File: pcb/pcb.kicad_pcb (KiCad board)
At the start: 2 copper layers, 100 x 70 mm, 20 parts, among them K1 GENERIC_RELAY, K2 GENERIC_RELAY, Q1 BC547, Q2 BC547

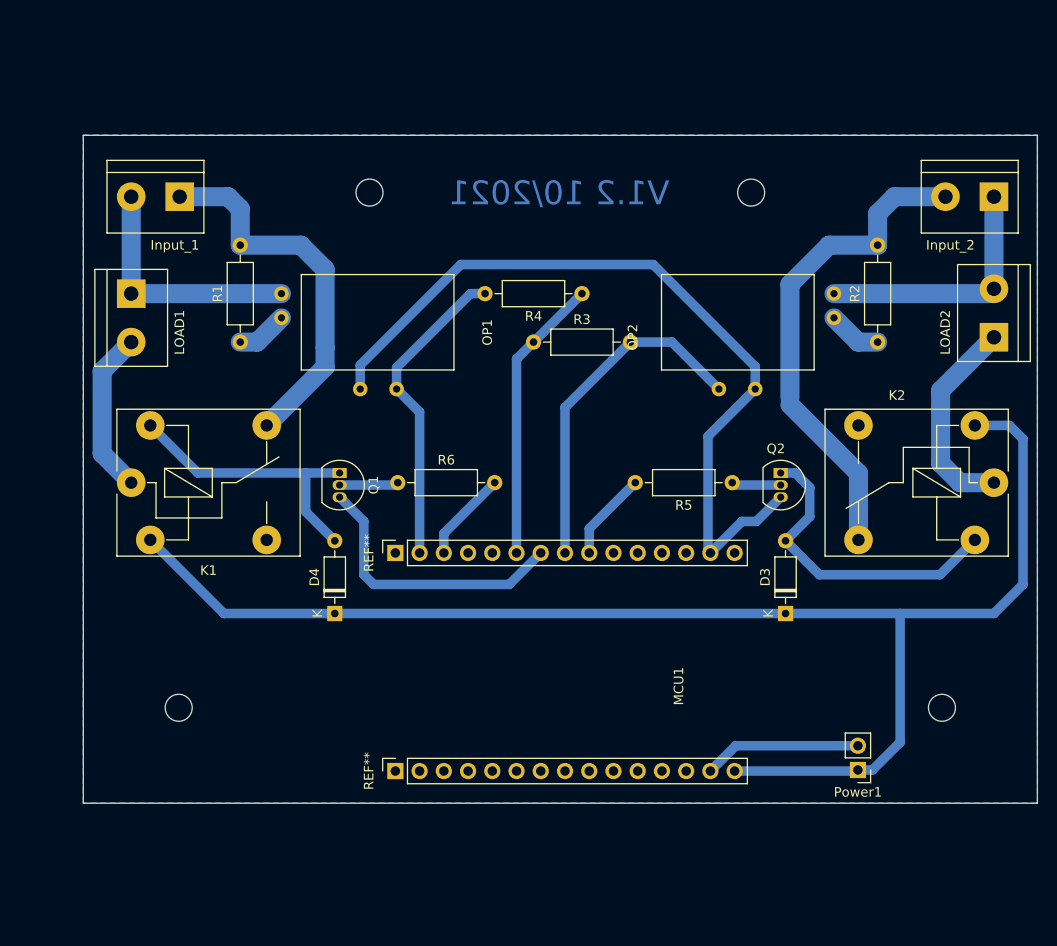
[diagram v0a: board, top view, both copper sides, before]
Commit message: Add new terminal block model and update PCB design
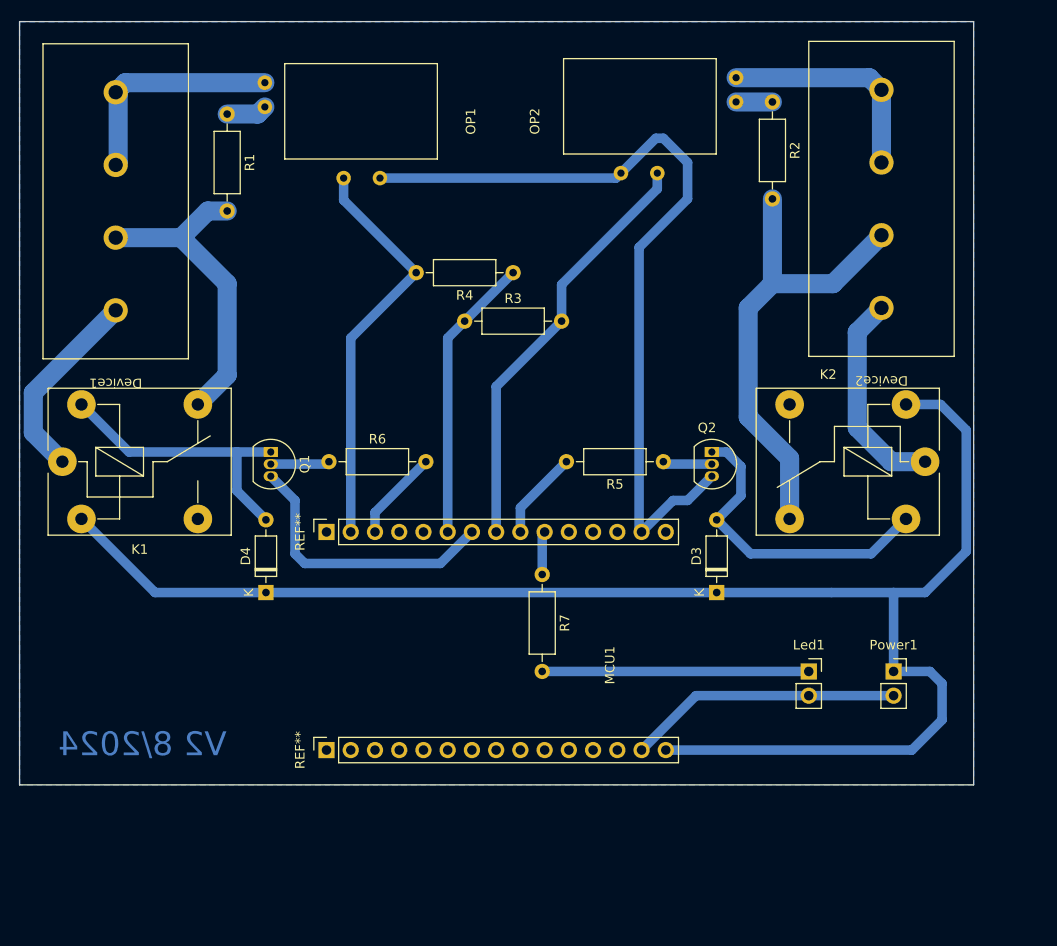
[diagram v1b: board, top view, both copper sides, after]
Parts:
- removed Input_1, Input_2, LOAD1, LOAD2: Conn_01x02, TerminalBlock:TerminalBlock_bornier-2_P5.08mm
- added Device1: Conn_01x04, Custom_Footprints:TerminalBlock_1x04, F.Cu at (100.1, 68.8)
- added Device2: Conn_01x04, Custom_Footprints:TerminalBlock_1x04, F.Cu at (180.3, 68.6)
- added Led1: Conn_01x02, Connector_PinSocket_2.54mm:PinSocket_1x02_P2.54mm_Vertical, F.Cu at (172.7, 118.1)
- added R7: 220, Resistor_THT:R_Axial_DIN0207_L6.3mm_D2.5mm_P10.16mm_Horizontal, F.Cu at (144.8, 108.0)
- K1, K2: value GENERIC_RELAY -> Generic_Relay
- Power1: footprint Connector_PinHeader_2.54mm:PinHeader_1x02_P2.54mm_Vertical -> Connector_PinSocket_2.54mm:PinSocket_1x02_P2.54mm_Vertical
- moved R2 27.5 mm to (168.9, 58.4), turned to -90 degrees
- moved OP2 24.9 mm to (147.3, 55.9)
- moved R1 23.9 mm to (111.8, 59.7), turned to -90 degrees
- moved OP1 22.2 mm to (134.0, 67.6)
- moved Power1 11.0 mm to (181.6, 118.1), turned to 0 degrees
- moved D4 7.54 mm to (115.8, 109.8)
- moved Q1 7.54 mm to (116.3, 95.1)
- moved Q2 7.54 mm to (162.6, 95.1)
- moved R4 7.54 mm to (141.7, 76.3)
- moved MCU1 7.54 mm to (151.4, 117.5)
- moved R3 7.54 mm to (136.7, 81.4)
- moved R5 7.54 mm to (157.5, 96.1)
- moved R6 7.54 mm to (122.4, 96.1)
- moved K1 7.54 mm to (94.5, 96.1)
- moved D3 7.54 mm to (163.1, 109.8)
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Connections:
- MCU1 pad 17: Net-(OP1-LDR2) -> Net-(OP1-LDR1)
- MCU1 pad 21: unconnected-(MCU1-D7-Pad21) -> Net-(MCU1-D7)
- OP1 pad 1: Net-(MCU1-D1) -> Net-(OP1-LDR1)
- OP1 pad 2: Net-(OP1-LDR2) -> Net-(MCU1-D1)
- OP2 pad 1: Net-(MCU1-D5) -> Net-(OP1-LDR1)
- OP2 pad 2: Net-(OP1-LDR2) -> Net-(MCU1-D5)
- Q2 pad 3: Net-(OP1-LDR2) -> Net-(OP1-LDR1)
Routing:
- net Net-(OP1-LDR1): track 0.00 -> 85.7 mm
- net Net-(OP1-LDR2): track 84.2 -> 0.00 mm
- net Net-(Led1-Pin_1): track 0.00 -> 27.9 mm
- net Net-(D3-K): track 148.9 -> 165.8 mm
- net Net-(Led1-Pin_2): track 16.6 -> 28.8 mm
- net Net-(MCU1-D1): track 32.9 -> 43.1 mm
- net Net-(MCU1-D5): track 36.2 -> 44.6 mm
- net Net-(Device1-Pin_3): track 39.5 -> 33.6 mm
- net Net-(MCU1-D7): track 0.00 -> 4.56 mm
- net Net-(Device1-Pin_4): track 17.3 -> 20.7 mm
- net Net-(Device2-Pin_1): track 26.6 -> 23.4 mm
- net Net-(Device1-Pin_1): track 25.9 -> 23.9 mm
- net Net-(Device2-Pin_3): track 51.8 -> 49.9 mm
- net Net-(OP2-IN1): track 5.62 -> 3.81 mm
- net Net-(OP1-IN1): track 5.37 -> 4.26 mm
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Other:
- board size 100 x 70 mm -> 100 x 80 mm
- board text added: "V2 8/2024"
- board text removed: "V1.2 10/2021"

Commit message: Add pin socket model and update PCB
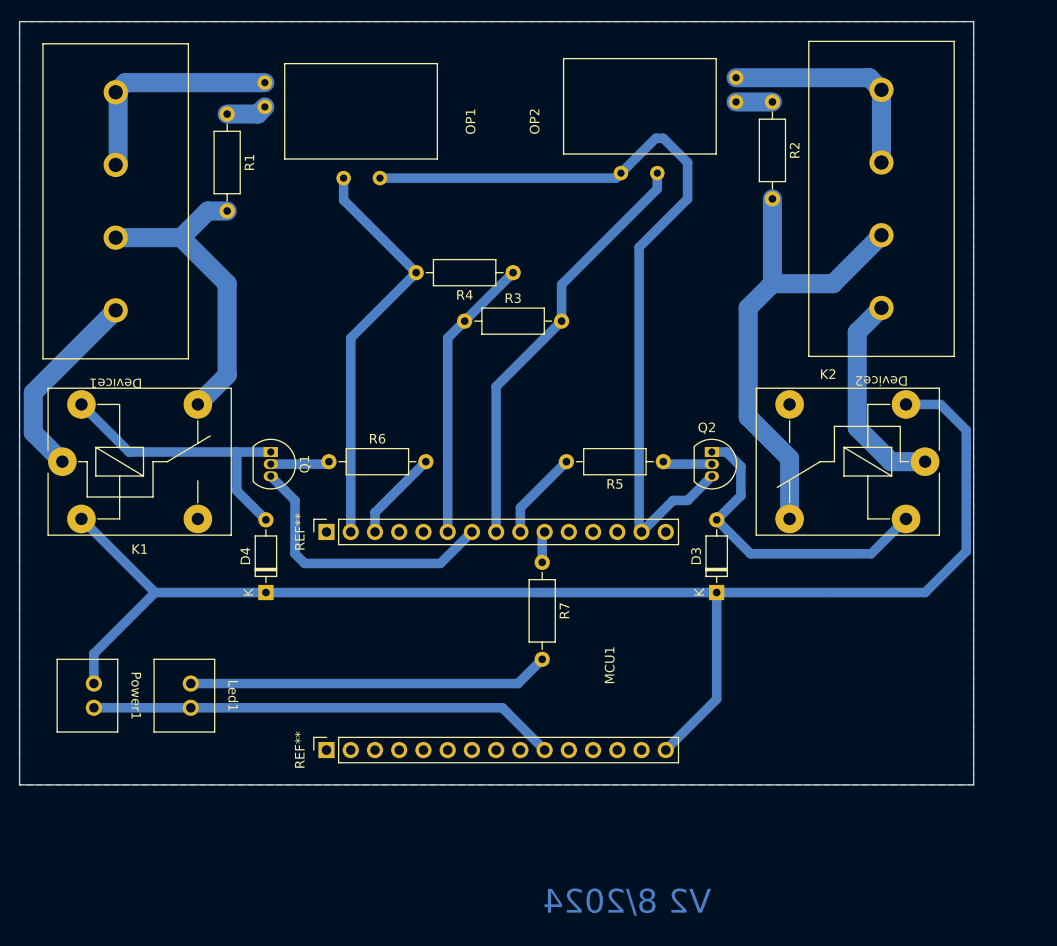
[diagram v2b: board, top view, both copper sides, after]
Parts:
- Led1, Power1: footprint Connector_PinSocket_2.54mm:PinSocket_1x02_P2.54mm_Vertical -> Custom_Footprints:PinSocket_1x02
- moved Power1 84.5 mm to (97.1, 120.7), turned to -90 degrees
- moved Led1 65.5 mm to (107.3, 120.7), turned to -90 degrees
- moved R7 1.27 mm to (144.8, 106.7)
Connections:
- MCU1 pad 10: unconnected-(MCU1-GND-Pad10) -> Net-(Led1-Pin_2)
- MCU1 pad 14: Net-(Led1-Pin_2) -> unconnected-(MCU1-GND-Pad14)
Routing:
- net Net-(Led1-Pin_2): track 28.8 -> 49.1 mm
- net Net-(D3-K): track 165.8 -> 148.8 mm
- net Net-(Led1-Pin_1): track 27.9 -> 37.9 mm
- net Net-(MCU1-D7): track 4.56 -> 3.29 mm

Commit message: Align footprints and PCB components placement
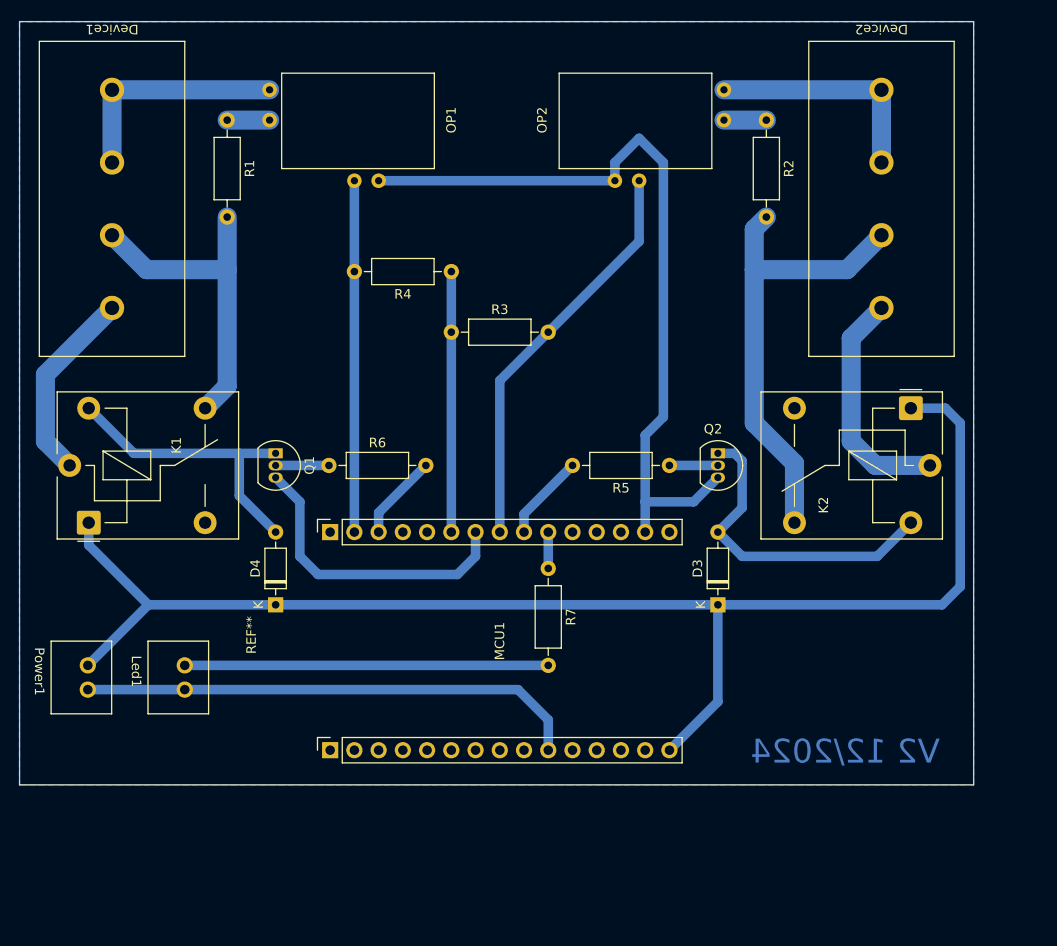
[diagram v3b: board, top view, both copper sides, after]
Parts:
- moved MCU1 30.2 mm to (122.6, 126.4)
- moved OP2 11.9 mm to (152.4, 66.7)
- moved Device1 11.7 mm to (99.7, 57.1)
- moved Device2 11.4 mm to (180.3, 57.1)
- moved K1 6.97 mm to (97.2, 102.5), turned to 90 degrees
- moved R4 6.48 mm to (135.3, 76.2)
- moved OP1 6.43 mm to (127.6, 66.7)
- moved K2 5.80 mm to (183.4, 90.5), turned to -90 degrees
- moved Power1 3.18 mm to (97.2, 117.5)
- moved Led1 3.18 mm to (107.3, 117.5)
- moved R2 2.01 mm to (168.3, 60.3)
- moved R3 1.81 mm to (135.3, 82.5)
- moved D4 1.64 mm to (116.8, 111.1)
- moved D3 1.29 mm to (163.2, 111.1)
- moved R7 0.90 mm to (145.4, 107.3)
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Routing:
- net Net-(MCU1-D1): track 43.1 -> 36.8 mm
- net Net-(Led1-Pin_2): track 49.1 -> 52.8 mm
- net Net-(OP1-LDR1): track 85.7 -> 82.8 mm
- net Net-(MCU1-3V3-Pad25): track 30.0 -> 27.3 mm
- net Net-(D3-K): track 148.8 -> 146.4 mm
- net Net-(Device2-Pin_4): track 22.2 -> 24.6 mm
- net Net-(Q1-E): track 29.5 -> 31.8 mm
- net Net-(MCU1-D5): track 44.6 -> 42.9 mm
- net Net-(D4-A): track 30.3 -> 31.4 mm
- net Net-(D3-A): track 33.1 -> 34.1 mm
- net Net-(Device1-Pin_3): track 33.6 -> 34.6 mm
- net Net-(Device2-Pin_3): track 49.9 -> 49.1 mm
- net Net-(Device2-Pin_1): track 23.4 -> 24.1 mm
- net Net-(OP2-IN1): track 3.81 -> 4.44 mm
- net Net-(Q1-B): track 6.20 -> 5.59 mm
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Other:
- board text added: "V2 12/2024"
- board text removed: "V2 8/2024"
